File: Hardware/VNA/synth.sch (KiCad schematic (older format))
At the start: 34 parts, among them U3 MAX2871, X1 ASTXR-12-19.200MHz

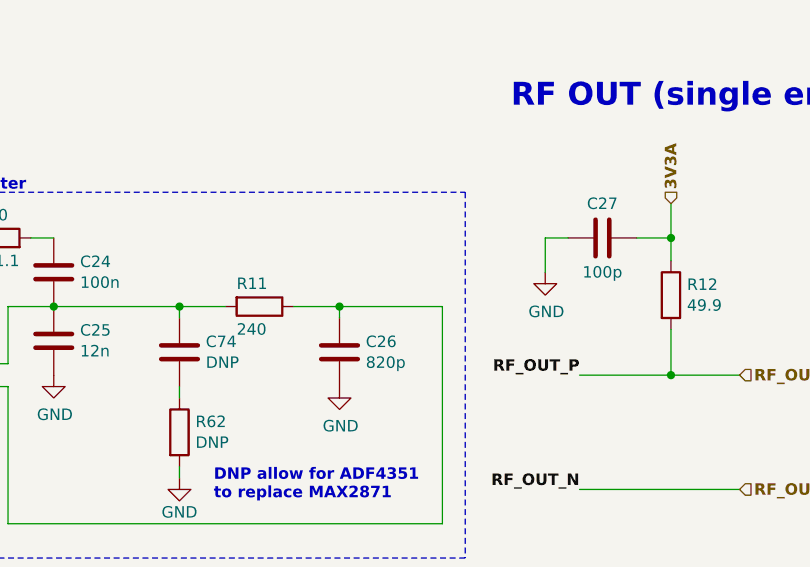
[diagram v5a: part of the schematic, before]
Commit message: Layout done, front and rear panels designed
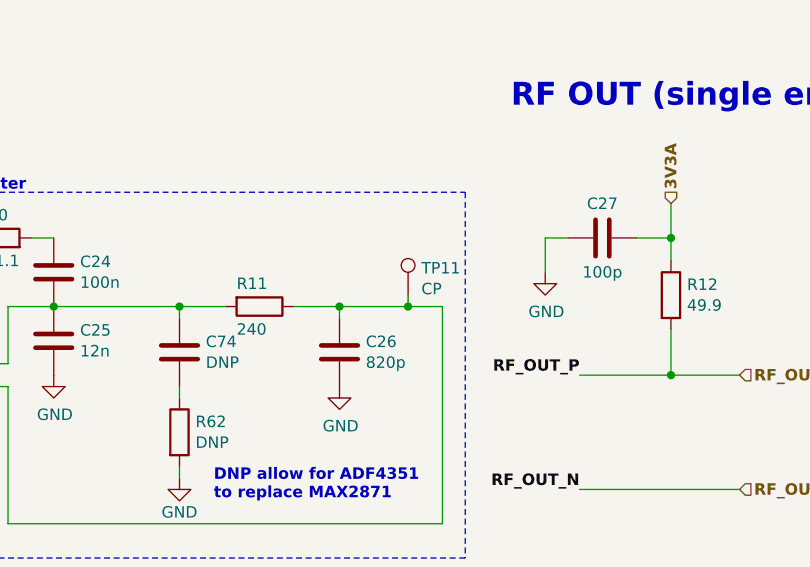
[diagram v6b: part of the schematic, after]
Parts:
- added TP11: CP, TestPoint:TestPoint_Pad_D1.0mm, symbol Connector:TestPoint
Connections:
- net at C26.1, R11.1, U3.20 (TUNE): now also TP11.1
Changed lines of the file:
@@
 	7100 4650 7100 5250
 Wire Wire Line
-	8550 4300 9000 4300
+	8550 4300 8850 4300
 $Comp
 L power:GND #PWR0124
@@
 Text Notes 8000 5150 0    50   ~ 10
 DNP allow for ADF4351\nto replace MAX2871
+$Comp
+L Connector:TestPoint TP11
+U 1 1 5CBE7782
+P 8850 4250
+F 0 "TP11" H 8908 4368 50  0000 L CNN
+F 1 "CP" H 8908 4277 50  0000 L CNN
+F 2 "TestPoint:TestPoint_Pad_D1.0mm" H 9050 4250 50  0001 C CNN
+F 3 "~" H 9050 4250 50  0001 C CNN
+	1    8850 4250
+	1    0    0    -1
+$EndComp
+Wire Wire Line
+	8850 4250 8850 4300
+Connection ~ 8850 4300
+Wire Wire Line
+	8850 4300 9000 4300
 $EndSCHEMATC

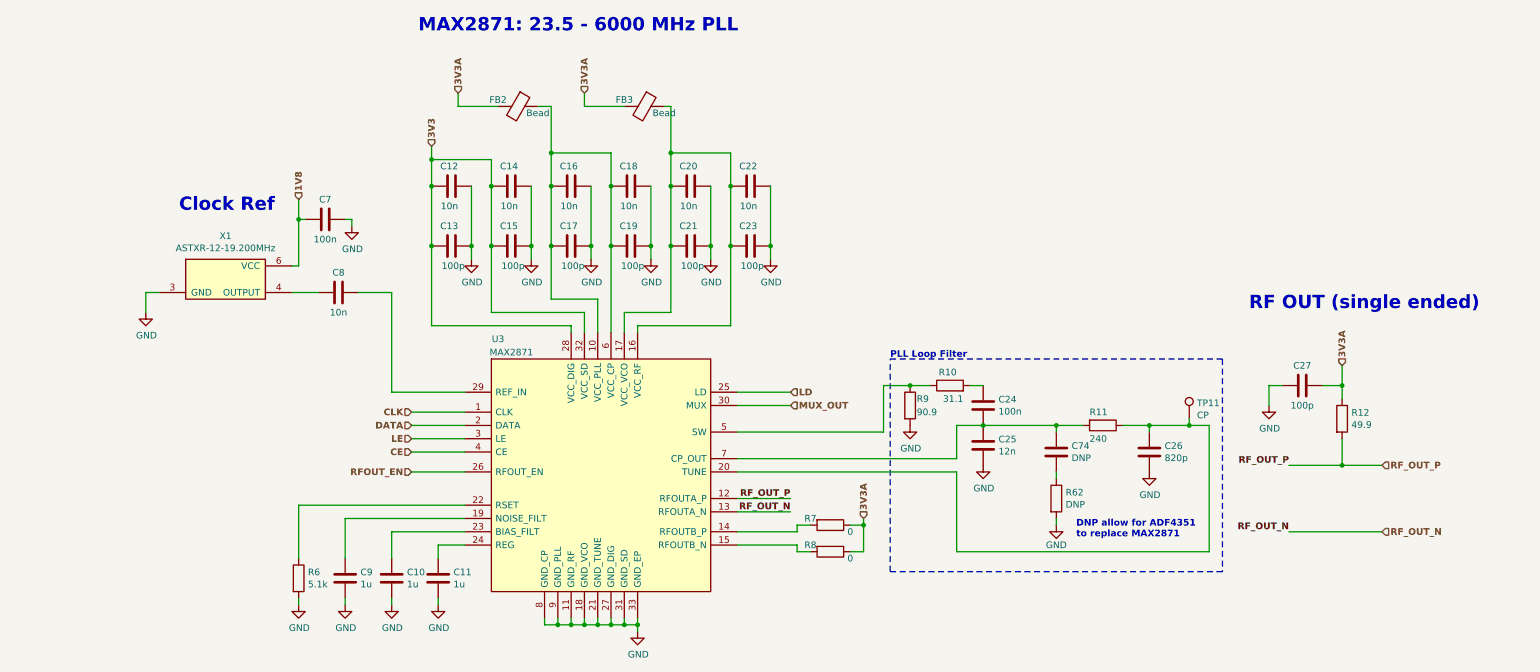
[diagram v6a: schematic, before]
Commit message: fix KiCad 5.1.0 bold after plot issue on schematics
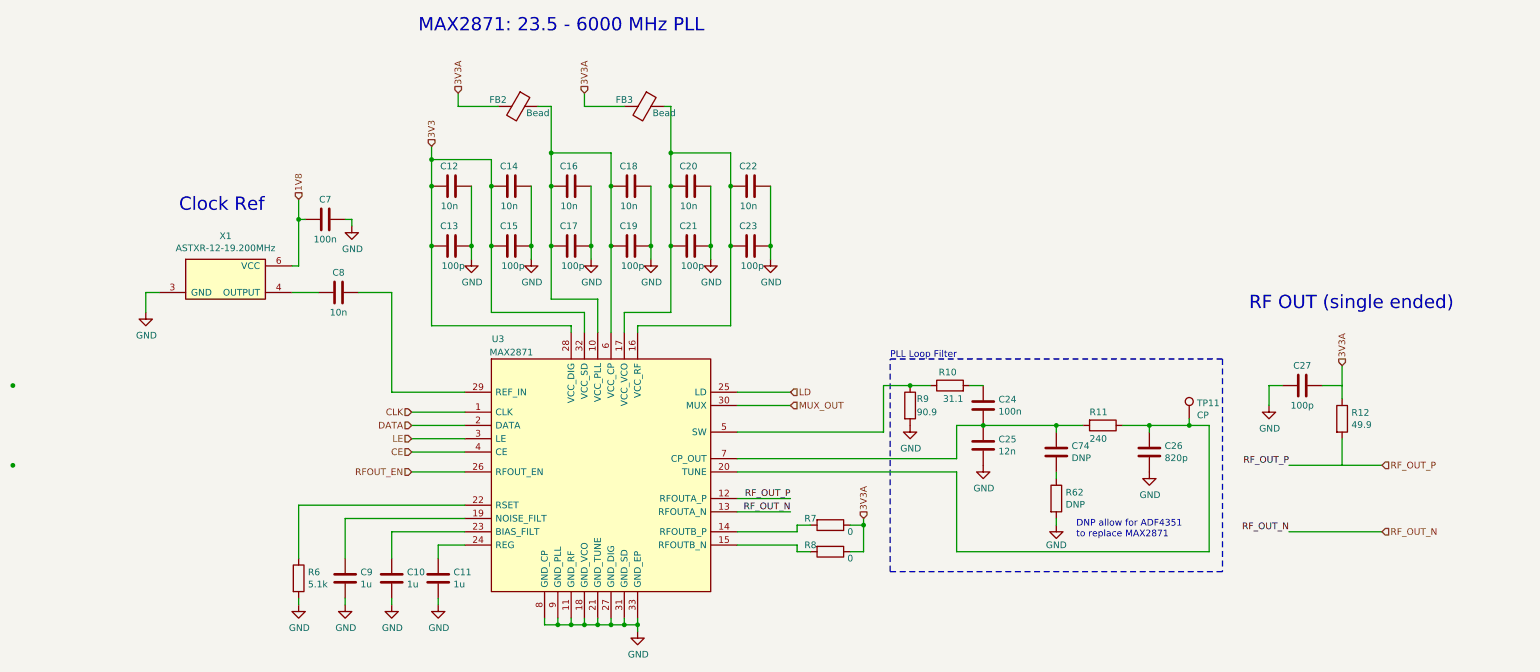
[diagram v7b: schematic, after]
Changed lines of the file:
@@
 Wire Notes Line
 	6600 5400 6600 3800
-Text Notes 6600 3800 0    50   ~ 10
+Text Notes 6600 3800 0    50   ~ 0
 PLL Loop Filter\n
 Wire Wire Line
@@
 Wire Wire Line
 	5450 4950 5850 4950
-Text Label 5850 4950 2    50   ~ 10
+Text Label 5850 4950 2    50   ~ 0
 RF_OUT_N
-Text Label 5850 4850 2    50   ~ 10
+Text Label 5850 4850 2    50   ~ 0
 RF_OUT_P
 Wire Wire Line
@@
 	4950 1900 4950 2250
 Connection ~ 4950 2250
-Text Label 9600 5100 2    50   ~ 10
+Text Label 9600 5100 2    50   ~ 0
 RF_OUT_N
-Text Label 9600 4600 2    50   ~ 10
+Text Label 9600 4600 2    50   ~ 0
 RF_OUT_P
 Wire Wire Line
@@
 	1    0    0    -1
 $EndComp
-Connection ~ 10000 4000
+Connection ~ 0000 4000
 Wire Wire Line
 	10000 4000 10000 4100
@@
 Wire Wire Line
 	5450 5100 5900 5100
-Text Notes 9300 3600 0    100  ~ 20
+Text Notes 9300 3600 0    100  ~ 0
 RF OUT (single ended)\n\n
 Wire Wire Line
@@
 	1    0    0    -1
 $EndComp
-Text Notes 1250 2700 0    100  ~ 20
+Text Notes 1250 2700 0    100  ~ 0
 Clock Ref\n
 Wire Wire Line
@@
 Wire Wire Line
 	10000 4400 10000 4600
-Connection ~ 10000 4600
+Connection ~ 0000 4600
 Wire Wire Line
 	10000 4600 10300 4600
@@
 Wire Wire Line
 	3150 2300 3150 2500
-Text HLabel 10300 4600 2    50   Input ~ 10
+Text HLabel 10300 4600 2    50   Input ~ 0
 RF_OUT_P
-Text HLabel 10300 5100 2    50   Input ~ 10
+Text HLabel 10300 5100 2    50   Input ~ 0
 RF_OUT_N
-Text HLabel 5850 4050 2    50   Input ~ 10
+Text HLabel 5850 4050 2    50   Input ~ 0
 LD
-Text HLabel 5850 4150 2    50   Input ~ 10
+Text HLabel 5850 4150 2    50   Input ~ 0
 MUX_OUT
-Text HLabel 3000 4200 0    50   Input ~ 10
+Text HLabel 3000 4200 0    50   Input ~ 0
 CLK
-Text HLabel 3000 4300 0    50   Input ~ 10
+Text HLabel 3000 4300 0    50   Input ~ 0
 DATA
-Text HLabel 3000 4400 0    50   Input ~ 10
+Text HLabel 3000 4400 0    50   Input ~ 0
 LE
-Text HLabel 3000 4500 0    50   Input ~ 10
+Text HLabel 3000 4500 0    50   Input ~ 0
 CE
-Text HLabel 3000 4650 0    50   Input ~ 10
+Text HLabel 3000 4650 0    50   Input ~ 0
 RFOUT_EN
 Connection ~ 3150 2500
@@
 	6750 4000 6900 4000
 Connection ~ 7300 4300
-Text Notes 3050 1350 0    100  ~ 20
+Text Notes 3050 1350 0    100  ~ 0
 MAX2871: 23.5 - 6000 MHz PLL\n
-Text HLabel 10000 3850 1    50   Input ~ 10
+Text HLabel 10000 3850 1    50   Input ~ 0
 3V3A
-Text HLabel 2150 2600 1    50   Input ~ 10
+Text HLabel 2150 2600 1    50   Input ~ 0
 1V8
-Text HLabel 3350 1800 1    50   Input ~ 10
+Text HLabel 3350 1800 1    50   Input ~ 0
 3V3A
-Text HLabel 4300 1800 1    50   Input ~ 10
+Text HLabel 4300 1800 1    50   Input ~ 0
 3V3A
-Text HLabel 6400 5000 1    50   Input ~ 10
+Text HLabel 6400 5000 1    50   Input ~ 0
 3V3A
-Text HLabel 3150 2200 1    50   Input ~ 10
+Text HLabel 3150 2200 1    50   Input ~ 0
 3V3
 $Comp
@@
 Wire Notes Line
 	9100 5400 6600 5400
-Text Notes 8000 5150 0    50   ~ 10
+Text Notes 8000 5150 0    50   ~ 0
 DNP allow for ADF4351\nto replace MAX2871
 $Comp
